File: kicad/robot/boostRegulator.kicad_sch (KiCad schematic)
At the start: 21 parts, among them U5 LSF0102DCTR, U6 MAX77857

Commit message: Exported all schematic symbols to local robot and refer to them in all symbols
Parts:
- C24, C25, C26, C27, C28, C29, C30, C31, C32, C33, C34, C74: symbol Device:C -> robot:C
- L1: symbol Device:L -> robot:L
- R19, R20, R21: symbol Device:R -> robot:R
- TP31, TP32, TP33: symbol Connector:TestPoint -> robot:TestPoint
- U5: symbol Logic_LevelTranslator:LSF0102DCTR -> robot:LSF0102DCTR
- U6: symbol Regulator_Switching:MAX77857 -> robot:MAX77857
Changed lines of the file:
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@@
     (effects (font (size 1.27 1.27)) (justify right))
   )
-  (symbol (lib_id "Regulator_Switching:MAX77857") (at 194.31 106.68 0) (unit 1)
+  (symbol (lib_id "robot:MAX77857") (at 194.31 106.68 0) (unit 1)
     (in_bom yes) (on_board yes) (dnp no)
     (property "Reference" "U6" (at 194.31 104.14 0)
@@
     )
   )
-  (symbol (lib_id "Device:C") (at 156.21 114.3 0) (unit 1)
+  (symbol (lib_id "robot:C") (at 156.21 114.3 0) (unit 1)
     (in_bom yes) (on_board yes) (dnp no)
     (property "Reference" "C28" (at 160.02 113.0299 0)
@@
     )
   )
-  (symbol (lib_id "Logic_LevelTranslator:LSF0102DCTR") (at 78.74 127 0) (mirror y) (unit 1)
+  (symbol (lib_id "robot:LSF0102DCTR") (at 78.74 127 0) (mirror y) (unit 1)
     (in_bom yes) (on_board yes) (dnp no) (fields_autoplaced)
     (property "Reference" "U5" (at 78.74 109.22 0)
@@
     )
   )
-  (symbol (lib_id "Device:C") (at 228.6 93.98 180) (unit 1)
+  (symbol (lib_id "robot:C") (at 228.6 93.98 180) (unit 1)
     (in_bom yes) (on_board yes) (dnp no)
     (property "Reference" "C32" (at 223.52 95.25 0)
@@
     )
   )
-  (symbol (lib_id "Device:C") (at 137.795 93.98 0) (unit 1)
+  (symbol (lib_id "robot:C") (at 137.795 93.98 0) (unit 1)
     (in_bom yes) (on_board yes) (dnp no)
     (property "Reference" "C27" (at 141.605 91.4399 0)
@@
     )
   )
-  (symbol (lib_id "Device:R") (at 109.22 115.57 0) (unit 1)
+  (symbol (lib_id "robot:R") (at 109.22 115.57 0) (unit 1)
     (in_bom yes) (on_board yes) (dnp no)
     (property "Reference" "R20" (at 111.76 114.2999 0)
@@
     )
   )
-  (symbol (lib_id "Device:C") (at 125.095 93.98 0) (unit 1)
+  (symbol (lib_id "robot:C") (at 125.095 93.98 0) (unit 1)
     (in_bom yes) (on_board yes) (dnp no) (fields_autoplaced)
     (property "Reference" "C25" (at 128.905 91.4399 0)
@@
     )
   )
-  (symbol (lib_id "Device:C") (at 44.45 120.65 0) (unit 1)
+  (symbol (lib_id "robot:C") (at 44.45 120.65 0) (unit 1)
     (in_bom yes) (on_board yes) (dnp no)
     (property "Reference" "C24" (at 48.26 119.3799 0)
@@
     )
   )
-  (symbol (lib_id "Connector:TestPoint") (at 96.52 129.54 0) (mirror x) (unit 1)
+  (symbol (lib_id "robot:TestPoint") (at 96.52 129.54 0) (mirror x) (unit 1)
     (in_bom yes) (on_board yes) (dnp no)
     (property "Reference" "TP32" (at 102.87 134.62 0)
@@
     )
   )
-  (symbol (lib_id "Connector:TestPoint") (at 228.6 97.79 270) (unit 1)
+  (symbol (lib_id "robot:TestPoint") (at 228.6 97.79 270) (unit 1)
     (in_bom yes) (on_board yes) (dnp no) (fields_autoplaced)
     (property "Reference" "TP33" (at 233.68 97.7899 90)
@@
     )
   )
-  (symbol (lib_id "Device:C") (at 153.035 93.98 180) (unit 1)
+  (symbol (lib_id "robot:C") (at 153.035 93.98 180) (unit 1)
     (in_bom yes) (on_board yes) (dnp no)
     (property "Reference" "C29" (at 158.115 91.44 0)
@@
     )
   )
-  (symbol (lib_id "Device:C") (at 254 93.98 180) (unit 1)
+  (symbol (lib_id "robot:C") (at 254 93.98 180) (unit 1)
     (in_bom yes) (on_board yes) (dnp no)
     (property "Reference" "C34" (at 248.92 95.25 0)
@@
     )
   )
-  (symbol (lib_id "Device:L") (at 195.58 73.66 90) (unit 1)
+  (symbol (lib_id "robot:L") (at 195.58 73.66 90) (unit 1)
     (in_bom yes) (on_board yes) (dnp no) (fields_autoplaced)
     (property "Reference" "L1" (at 195.58 67.31 90)
@@
     )
   )
-  (symbol (lib_id "Connector:TestPoint") (at 96.52 127 0) (unit 1)
+  (symbol (lib_id "robot:TestPoint") (at 96.52 127 0) (unit 1)
     (in_bom yes) (on_board yes) (dnp no) (fields_autoplaced)
     (property "Reference" "TP31" (at 99.06 123.6979 0)
@@
     )
   )
-  (symbol (lib_id "Device:C") (at 241.3 93.98 180) (unit 1)
+  (symbol (lib_id "robot:C") (at 241.3 93.98 180) (unit 1)
     (in_bom yes) (on_board yes) (dnp no)
     (property "Reference" "C33" (at 236.22 95.25 0)
@@
     )
   )
-  (symbol (lib_id "Device:C") (at 184.15 73.66 90) (unit 1)
+  (symbol (lib_id "robot:C") (at 184.15 73.66 90) (unit 1)
     (in_bom yes) (on_board yes) (dnp no)
     (property "Reference" "C30" (at 184.15 66.04 90)
@@
     )
   )
-  (symbol (lib_id "Device:R") (at 57.15 120.65 0) (unit 1)
+  (symbol (lib_id "robot:R") (at 57.15 120.65 0) (unit 1)
     (in_bom yes) (on_board yes) (dnp no) (fields_autoplaced)
     (property "Reference" "R19" (at 59.69 119.3799 0)
@@
     )
   )
-  (symbol (lib_id "Device:C") (at 144.78 107.95 0) (unit 1)
+  (symbol (lib_id "robot:C") (at 144.78 107.95 0) (unit 1)
     (in_bom yes) (on_board yes) (dnp no)
     (property "Reference" "C26" (at 148.59 106.6799 0)
@@
     )
   )
-  (symbol (lib_id "Device:C") (at 205.74 73.66 90) (unit 1)
+  (symbol (lib_id "robot:C") (at 205.74 73.66 90) (unit 1)
     (in_bom yes) (on_board yes) (dnp no)
     (property "Reference" "C31" (at 205.74 66.04 90)
@@
     )
   )
-  (symbol (lib_id "Device:R") (at 118.11 115.57 0) (unit 1)
+  (symbol (lib_id "robot:R") (at 118.11 115.57 0) (unit 1)
     (in_bom yes) (on_board yes) (dnp no) (fields_autoplaced)
     (property "Reference" "R21" (at 120.65 114.2999 0)
@@
     )
   )
-  (symbol (lib_id "Device:C") (at 266.7 93.98 0) (mirror y) (unit 1)
+  (symbol (lib_id "robot:C") (at 266.7 93.98 0) (mirror y) (unit 1)
     (in_bom no) (on_board yes) (dnp yes)
     (property "Reference" "C74" (at 262.89 91.4399 0)

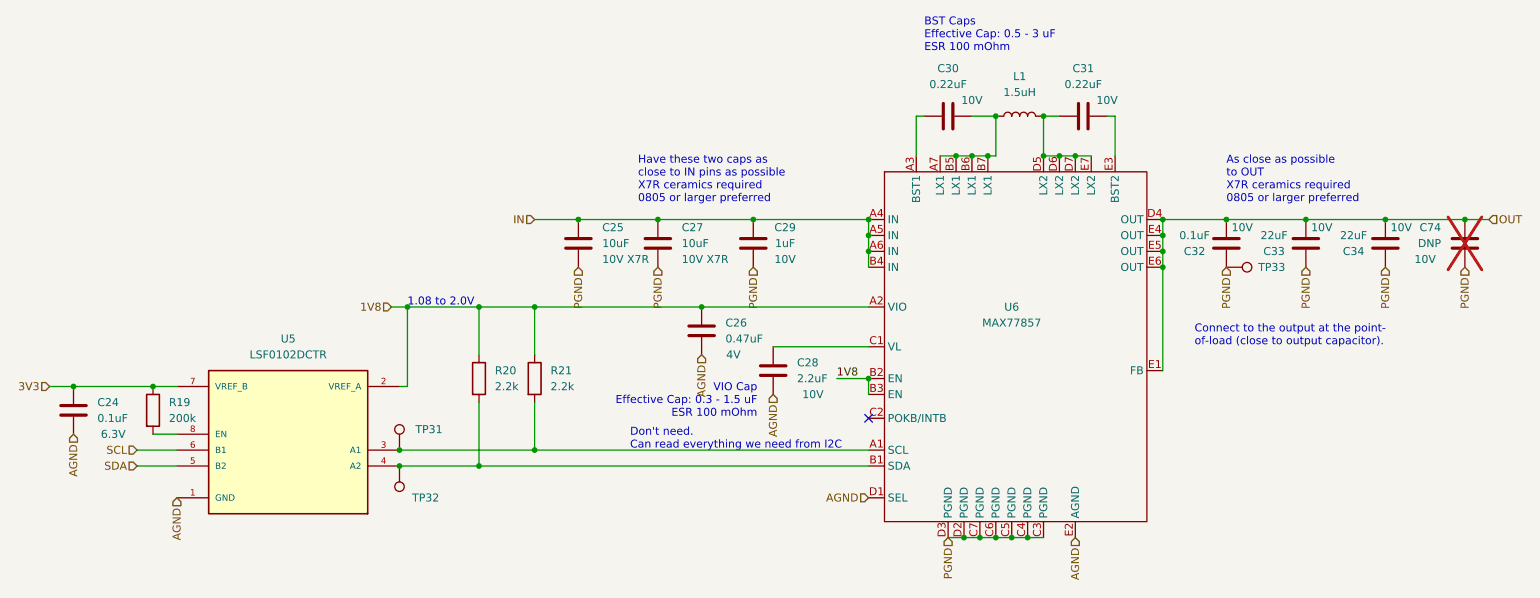
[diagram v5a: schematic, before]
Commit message: Replaced all test points with SMD parts where possible
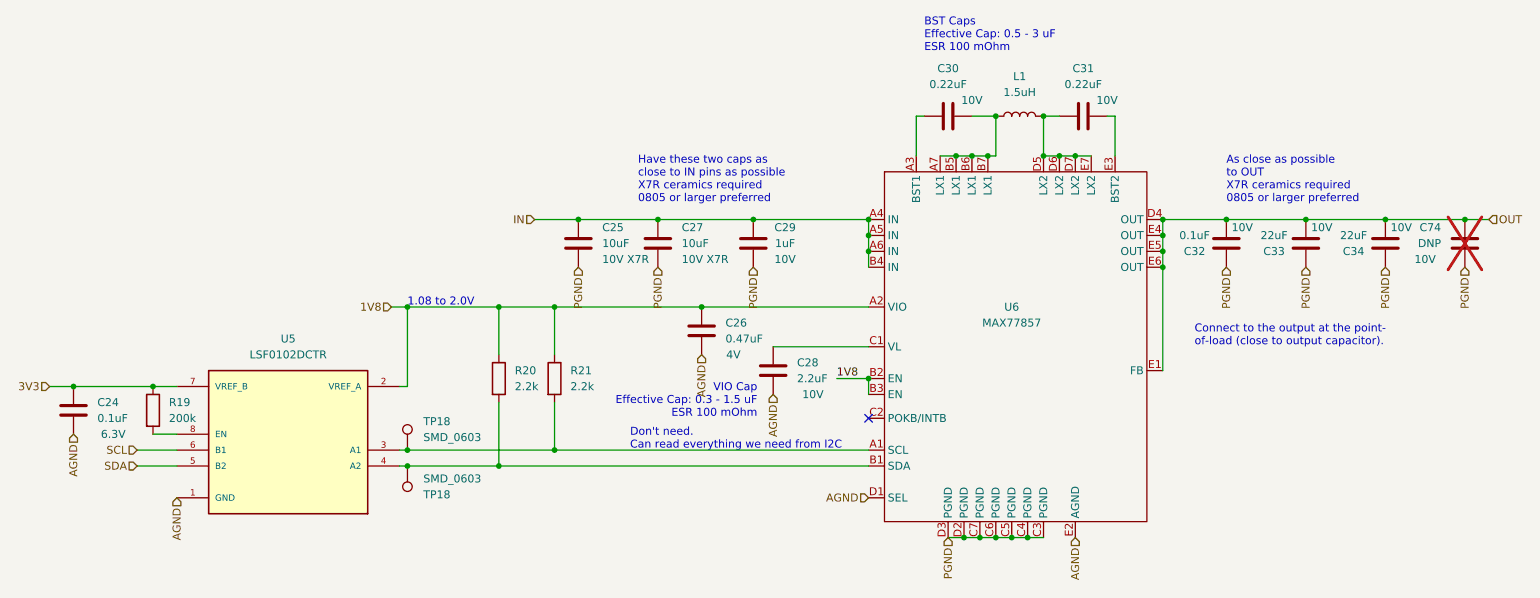
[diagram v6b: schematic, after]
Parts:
- removed TP31, TP32, TP33: TestPoint, robot:KEYSTONE_5002, symbol robot:TestPoint
- added TP18 (x2): SMD_0603, robot:TestPoint_SMD_0603, symbol robot:TestPoint
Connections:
- net at R21.2, U5.3 (A1), U6.A1 (SCL): now also TP18.1
- net at R20.2, U5.4 (A2), U6.B1 (SDA): now also TP18.1
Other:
- moved on the sheet: R20, R21

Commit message: Removing a bunch of unneccesary symbol properties
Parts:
- U5: MAXIMUM_PACKAGE_HEIGHT 1.3 mm -> (none); PARTREV J -> (none); STANDARD IPC-7351B -> (none); Stock 25 -> (none)
- U6: Stock 25 -> (none)
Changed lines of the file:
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@@
-      (effects (font (size 1.27 1.27)) hide)
-    )
-    (property "Stock" "25" (at 194.31 106.68 0)
       (effects (font (size 1.27 1.27)) hide)
     )
@@
       (effects (font (size 1.27 1.27)) (justify left bottom) hide)
     )
-    (property "PARTREV" "J" (at 78.74 127 0)
-      (effects (font (size 1.27 1.27)) (justify left bottom) hide)
-    )
-    (property "STANDARD" "IPC-7351B" (at 78.74 127 0)
-      (effects (font (size 1.27 1.27)) (justify left bottom) hide)
-    )
-    (property "MANUFACTURER" "" (at 78.74 127 0)
-      (effects (font (size 1.27 1.27)) (justify left bottom) hide)
-    )
-    (property "MAXIMUM_PACKAGE_HEIGHT" "1.3 mm" (at 78.74 127 0)
-      (effects (font (size 1.27 1.27)) (justify left bottom) hide)
-    )
     (property "Manufacturer" "Texas Instruments" (at 78.74 127 0)
       (effects (font (size 1.27 1.27)) hide)
@@
       (effects (font (size 1.27 1.27)) hide)
     )
-    (property "Stock" "25" (at 78.74 127 0)
-      (effects (font (size 1.27 1.27)) hide)
-    )

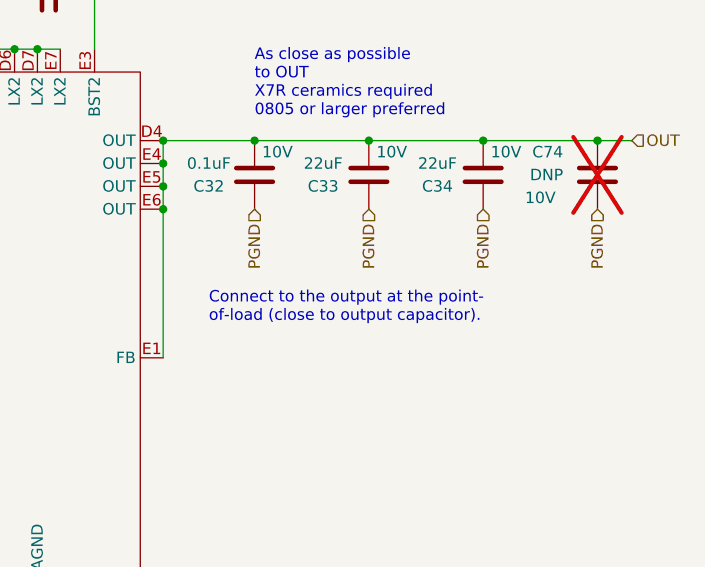
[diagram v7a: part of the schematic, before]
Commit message: Added power_2A net classes and net ties to schematic
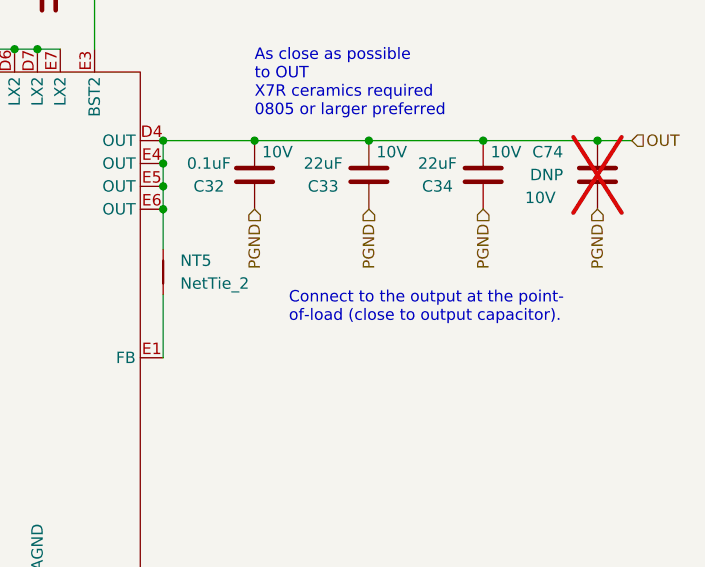
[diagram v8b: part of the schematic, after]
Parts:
- added NT5: NetTie_2, robot:NetTie-_SMD_Pad6mil, symbol Device:NetTie_2
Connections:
- net OUT: now also NT5.1; no longer U6.E1 (FB)
- new net: NT5.2, U6.E1 (FB)
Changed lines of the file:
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@@
   (junction (at 153.035 90.17) (diameter 0) (color 0 0 0 0)
   )
+  (junction (at 44.45 116.84) (diameter 0) (color 0 0 0 0)
+  )
+  (junction (at 191.77 140.97) (diameter 0) (color 0 0 0 0)
+  )
+  (junction (at 186.69 140.97) (diameter 0) (color 0 0 0 0)
+  )
+  (junction (at 144.78 104.14) (diameter 0) (color 0 0 0 0)
+  )
+  (junction (at 187.96 80.01) (diameter 0) (color 0 0 0 0)
+  )
+  (junction (at 189.23 140.97) (diameter 0) (color 0 0 0 0)
+  )
+  (junction (at 191.77 73.66) (diameter 0) (color 0 0 0 0)
+  )
+  (junction (at 266.7 90.17) (diameter 0) (color 0 0 0 0)
+  )
+  (junction (at 171.45 115.57) (diameter 0) (color 0 0 0 0)
+  )
+  (junction (at 196.85 140.97) (diameter 0) (color 0 0 0 0)
+  )
+  (junction (at 121.285 104.14) (diameter 0) (color 0 0 0 0)
+  )
   (junction (at 218.44 97.79) (diameter 0) (color 0 0 0 0)
-  )
-  (junction (at 44.45 116.84) (diameter 0) (color 0 0 0 0)
-  )
-  (junction (at 191.77 140.97) (diameter 0) (color 0 0 0 0)
-  )
-  (junction (at 186.69 140.97) (diameter 0) (color 0 0 0 0)
-  )
-  (junction (at 144.78 104.14) (diameter 0) (color 0 0 0 0)
-  )
-  (junction (at 187.96 80.01) (diameter 0) (color 0 0 0 0)
-  )
-  (junction (at 189.23 140.97) (diameter 0) (color 0 0 0 0)
-  )
-  (junction (at 191.77 73.66) (diameter 0) (color 0 0 0 0)
-  )
-  (junction (at 266.7 90.17) (diameter 0) (color 0 0 0 0)
-  )
-  (junction (at 171.45 115.57) (diameter 0) (color 0 0 0 0)
-  )
-  (junction (at 196.85 140.97) (diameter 0) (color 0 0 0 0)
-  )
-  (junction (at 121.285 104.14) (diameter 0) (color 0 0 0 0)
   )
   (junction (at 199.39 80.01) (diameter 0) (color 0 0 0 0)
@@
     (stroke (width 0) (type default))
   )
+  (wire (pts (xy 218.44 97.79) (xy 218.44 102.235))
+    (stroke (width 0) (type default))
+  )
   (wire (pts (xy 199.39 73.66) (xy 201.93 73.66))
     (stroke (width 0) (type default))
@@
     (stroke (width 0) (type default))
   )
-  (wire (pts (xy 218.44 97.79) (xy 218.44 114.3))
-    (stroke (width 0) (type default))
-  )
   (wire (pts (xy 153.035 90.17) (xy 171.45 90.17))
     (stroke (width 0) (type default))
@@
   )
   (wire (pts (xy 121.285 111.76) (xy 121.285 104.14))
+    (stroke (width 0) (type default))
+  )
+  (wire (pts (xy 218.44 107.315) (xy 218.44 114.3))
     (stroke (width 0) (type default))
   )
@@
   )
   (text "Connect to the output at the point-\nof-load (close to output capacitor)."
-    (at 223.52 110.49 0)
+    (at 232.41 110.49 0)
     (effects (font (size 1.27 1.27)) (justify left bottom))
   )
@@
   (hierarchical_label "SCL" (shape input) (at 54.61 127 180) (fields_autoplaced)
     (effects (font (size 1.27 1.27)) (justify right))
+  )
+  (netclass_flag "" (length 2.54) (shape round) (at 191.77 76.835 90) (fields_autoplaced)
+    (effects (font (size 1.27 1.27)) (justify left bottom))
+    (property "Netclass" "power_2A" (at 189.23 76.1365 90)
+      (effects (font (size 1.27 1.27) italic) (justify left) hide)
+    )
+  )
+  (netclass_flag "" (length 2.54) (shape round) (at 210.82 73.66 270) (fields_autoplaced)
+    (effects (font (size 1.27 1.27)) (justify right bottom))
+    (property "Netclass" "power_2A" (at 213.36 72.9615 90)
+      (effects (font (size 1.27 1.27) italic) (justify left) hide)
+    )
+  )
+  (netclass_flag "" (length 2.54) (shape round) (at 199.39 76.835 90) (fields_autoplaced)
+    (effects (font (size 1.27 1.27)) (justify left bottom))
+    (property "Netclass" "power_2A" (at 196.85 76.1365 90)
+      (effects (font (size 1.27 1.27) italic) (justify left) hide)
+    )
+  )
+  (netclass_flag "" (length 2.54) (shape round) (at 179.07 73.66 90) (fields_autoplaced)
+    (effects (font (size 1.27 1.27)) (justify left bottom))
+    (property "Netclass" "power_2A" (at 176.53 72.9615 90)
+      (effects (font (size 1.27 1.27) italic) (justify left) hide)
+    )
+  )
+  (netclass_flag "" (length 2.54) (shape round) (at 223.52 90.17 0) (fields_autoplaced)
+    (effects (font (size 1.27 1.27)) (justify left bottom))
+    (property "Netclass" "power_2A" (at 224.2185 87.63 0)
+      (effects (font (size 1.27 1.27) italic) (justify left) hide)
+    )
   )
   (symbol (lib_id "robot:MAX77857") (at 194.31 106.68 0) (unit 1)
@@
         )
       )
+    )
+  )
+  (symbol (lib_id "Device:NetTie_2") (at 218.44 104.775 270) (unit 1)
+    (in_bom no) (on_board yes) (dnp no)
+    (property "Reference" "NT5" (at 220.345 103.505 90)
+      (effects (font (size 1.27 1.27)) (justify left))
+    )
+    (property "Value" "NetTie_2" (at 220.345 106.045 90)
+      (effects (font (size 1.27 1.27)) (justify left))
+    )
+    (property "Footprint" "robot:NetTie-_SMD_Pad6mil" (at 218.44 104.775 0)
+      (effects (font (size 1.27 1.27)) hide)
+    )
+    (property "Datasheet" "~" (at 218.44 104.775 0)
+      (effects (font (size 1.27 1.27)) hide)
+    )
+    (pin "1")
+    (pin "2")
+    (instances
+      (project "robot"
+        (path "/0c7b298e-2d07-4b1f-b033-e95f02d45089/3fab603d-ed65-41bd-8de1-51639e39cb06"
+          (reference "NT5") (unit 1)
+        )
+        (path "/0c7b298e-2d07-4b1f-b033-e95f02d45089/aaf20b87-68dc-43c9-a7d3-4ceda8b87424"
+          (reference "NT15") (unit 1)
+        )
+        (path "/0c7b298e-2d07-4b1f-b033-e95f02d45089/427922e5-a943-4728-8788-709c0c3b2395"
+          (reference "NT15") (unit 1)
+        )
+      )
